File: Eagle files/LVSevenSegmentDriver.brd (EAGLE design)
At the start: 100 x 80 mm, 20 parts, among them IC1 74HC595D

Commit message: Ready for Fabbing
Silk Screens added and last minute DRC checks done.
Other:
- board text added: "LV 7 Seg Driver Alan F - V1.0"
- board text added: "LazerTag"
- board text removed: "7 Seg Driver Alan F - V1.0"
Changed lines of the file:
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@@
 <text x="46.99" y="23.495" size="0.889" layer="22" rot="MR180">GND</text>
 <text x="48.895" y="40.64" size="0.889" layer="22" rot="MR270">GND</text>
-<text x="41.91" y="27.305" size="0.762" layer="22" rot="MR270">7 Seg Driver
+<text x="41.91" y="27.305" size="0.762" layer="22" rot="MR270">LV 7 Seg Driver
 Alan F - V1.0</text>
+<text x="48.895" y="37.465" size="1.778" layer="22" rot="MR270">LazerTag</text>
 </plain>
 <attributes>

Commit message: Fixes
Removed outer footprint of board so that each board is now the correct
size instead of that of the default footprint.
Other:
- board size 100 x 80 mm -> 18.4 x 25.4 mm
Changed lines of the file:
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@@
 <board>
 <plain>
-<wire x1="0" y1="0" x2="100" y2="0" width="0" layer="20"/>
-<wire x1="100" y1="0" x2="100" y2="80" width="0" layer="20"/>
-<wire x1="100" y1="80" x2="0" y2="80" width="0" layer="20"/>
-<wire x1="0" y1="80" x2="0" y2="0" width="0" layer="20"/>
 <wire x1="39.37" y1="44.45" x2="39.37" y2="19.05" width="0.2032" layer="20"/>
 <wire x1="57.785" y1="21.59" x2="57.785" y2="44.45" width="0.2032" layer="20"/>

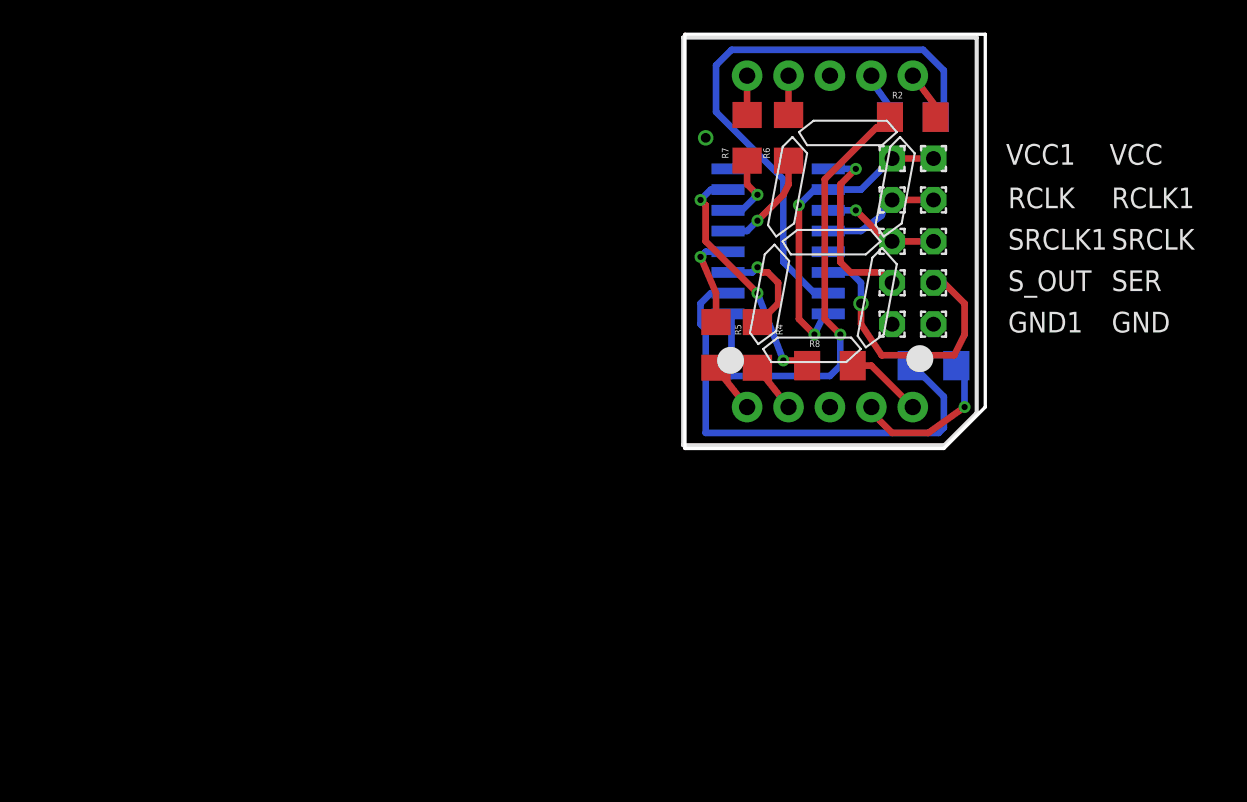
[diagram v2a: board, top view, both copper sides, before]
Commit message: aaaaaaaaaaaaaaaaaaaaaaaaaaaaaaaaaaaa
Cleaned up schematics, replaced wire solder points with header pin
mounts for standardization, recreated a broken file and dealt with the
confusion and insanity that followed.
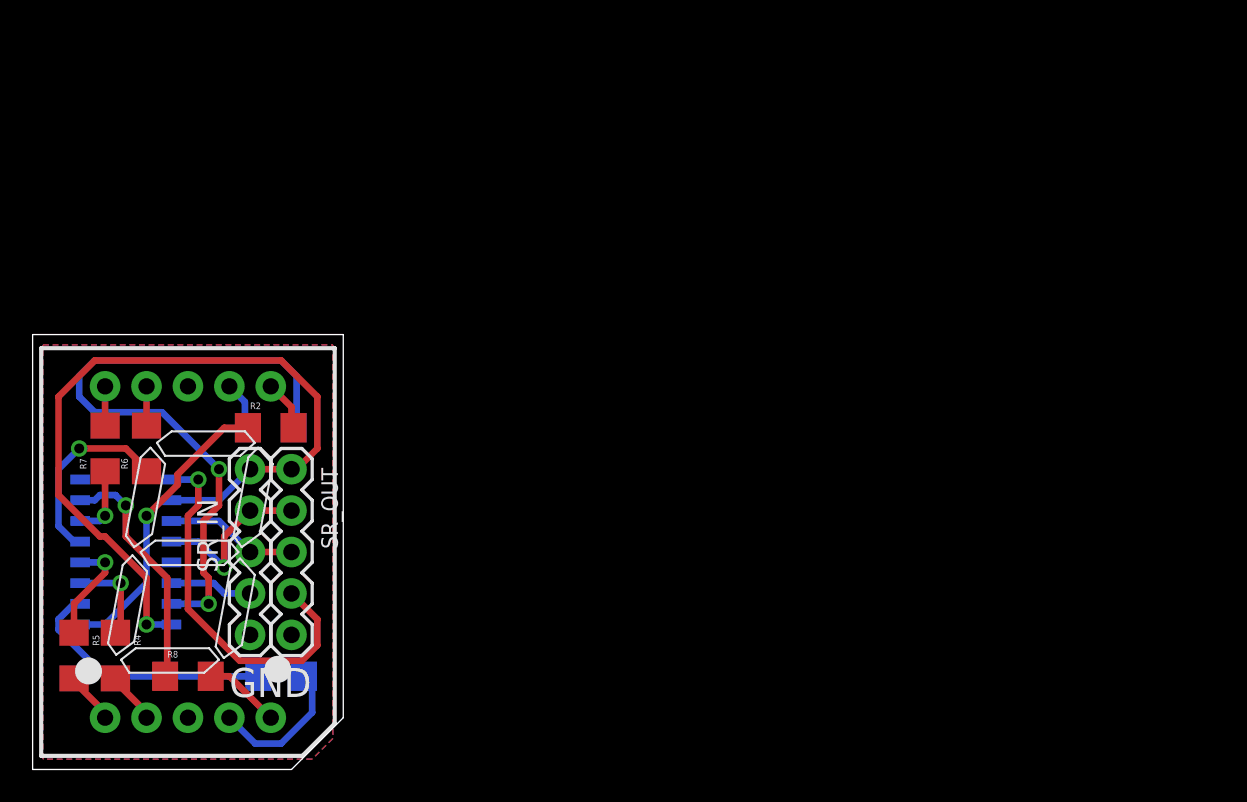
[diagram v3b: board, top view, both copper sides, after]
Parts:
- removed GND, GND1, RCLK, RCLK1, SER, SRCLK, SRCLK1, S_OUT: WIREPAD1,6/0,9, wirepad:1,6/0,9
- removed VCC, VCC1: WIREPAD1,6/0,9, smallestWirepadSquare:1,6/0,9
- added SR_IN, SR_OUT: (no value), SparkFun-Connectors:1X05
- IC1: value 74HC595D -> 74LS595D; device 74xx-eu:SO16 -> SparkFun-DigitalIC:SO16
- R1, R2, R3, R4, R5, R6, R7, R8: value 68 -> (none); device SparkFun-Passives:1206 -> SparkFun-Resistors:1206
- moved IC1 44.3 mm to (5.08, 12.7)
- moved R3 44.3 mm to (14.6, 5.08)
- moved R1 43.7 mm to (14.0, 20.3)
- moved R2 43.7 mm to (14.0, 20.3)
- moved R4 43.7 mm to (4.45, 6.35)
- moved R5 43.7 mm to (1.91, 6.35)
- moved R6 43.7 mm to (6.35, 19.1)
- moved R7 43.7 mm to (3.81, 19.1)
- moved R8 43.7 mm to (8.89, 5.08)
- moved U$1 43.7 mm to (8.89, 12.7)
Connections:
- removed net N$11 (its old number): IC1.9, S_OUT.1
- removed net N$12 (its old number): IC1.12, RCLK.1, RCLK1.1
- removed net N$13 (its old number): IC1.11, SRCLK.1, SRCLK1.1
- removed net N$14 (its old number): IC1.SER, SER.1
- new net RCLK: IC1.12, SR_IN.2, SR_OUT.2
- new net SCLK: IC1.11, SR_IN.3, SR_OUT.3
- new net SER_IN: IC1.14, SR_IN.4
- new net SER_OUT: IC1.9, SR_OUT.4
- net GND: now also SR_IN.5, SR_OUT.5; no longer GND.1, GND1.1
- net VCC: now also SR_IN.1, SR_OUT.1; no longer VCC.1, VCC1.1
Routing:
- net VCC: track 19.4 -> 49.1 mm, vias 2 -> 1
- net SER_OUT: track 0.00 -> 23.3 mm, vias 0 -> 1
- net N$14 (its old number): track 17.3 -> 0.00 mm, vias 1 -> 0
- net N$5: track 30.0 -> 15.8 mm
- net N$11 (its old number): track 11.5 -> 0.00 mm, vias 1 -> 0
- net N$3: track 29.3 -> 18.1 mm
- net RCLK: track 0.00 -> 10.6 mm, vias 0 -> 1
- net SCLK: track 0.00 -> 8.15 mm
- net N$12 (its old number): track 7.46 -> 0.00 mm
- net N$13 (its old number): track 7.18 -> 0.00 mm, vias 1 -> 0
- net N$11: track 6.48 -> 11.8 mm
- net SER_IN: track 0.00 -> 5.08 mm
- net N$1: track 35.5 -> 40.2 mm, vias 0 -> 2
- net N$7: track 6.61 -> 5.66 mm
- net N$6: track 9.95 -> 9.25 mm, vias 1 -> 0
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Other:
- board size 18.4 x 25.4 mm -> 19.1 x 26.7 mm
- board text removed: "A"
- board text removed: "B"
- board text removed: "C"
- board text removed: "D"
- board text removed: "DP"
- board text removed: "E"
- board text removed: "F"
- board text removed: "G"
- board text removed: "IC1"
- board text removed: "LV 7 Seg Driver Alan F - V1.0"
- board text removed: "LazerTag"
- board text removed: "RC"
- board text removed: "SI"
- board text removed: "SO"
- board text removed: "SR"
- board text removed: "VCC"

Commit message: Super Fresh
These boards are damn sexy.
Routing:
- net N$15: track 14.9 -> 16.8 mm
- net N$1: track 40.2 -> 41.7 mm
- net N$7: track 5.66 -> 4.35 mm
